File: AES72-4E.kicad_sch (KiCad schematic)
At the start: 5 parts, among them J101 NSJ12HC, J102 NSJ12HC, J103 NE8FAH

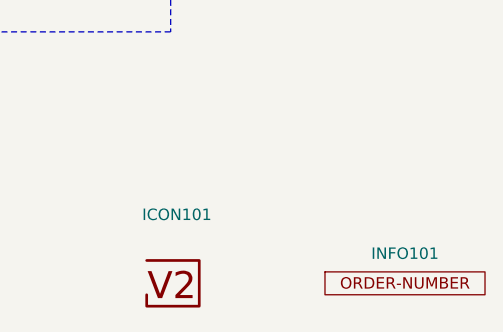
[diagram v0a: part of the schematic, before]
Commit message: Replace Order_Number
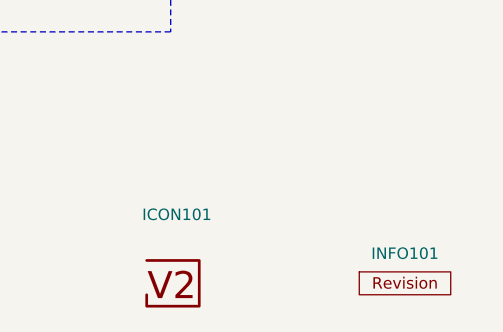
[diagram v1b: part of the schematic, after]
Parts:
- INFO101: value Order_Number -> ~; footprint V2_Production:Order_Number -> V2_Production:Revision; symbol V2_Production:Order_Number -> V2_Production:Revision
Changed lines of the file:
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@@
 	)
 	(symbol
-		(lib_id "V2_Production:Order_Number")
+		(lib_id "V2_Production:Revision")
 		(at 266.7 176.53 0)
 		(unit 1)
@@
 			)
 		)
-		(property "Value" "Order_Number"
+		(property "Value" "~"
 			(at 266.7 179.07 0)
 			(effects
@@
 			)
 		)
-		(property "Footprint" "V2_Production:Order_Number"
+		(property "Footprint" "V2_Production:Revision"
 			(at 266.7 181.61 0)
 			(effects
@@
 		(at 241.3 176.53 0)
 		(unit 1)
-		(exclude_from_sim yes)
+		(exclude_from_sim no)
 		(in_bom no)
 		(on_board yes)
